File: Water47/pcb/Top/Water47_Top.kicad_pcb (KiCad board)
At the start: 2 copper layers, 260 x 76.5 mm, 53 parts, among them SW1 Esc, SW10 O, SW11 P, SW12 -, SW13 Del, SW14 Cmd, SW15 A, SW16 S, SW17 D, SW18 F, SW19 G, SW2 Q, SW20 H, SW21 J, SW22 K, SW23 L, SW24 ;, SW25 Bs, SW26 Shift(L), SW27 Z, SW28 X, SW29 C, SW3 W, SW30 V, SW31 B, SW32 N, SW33 M, SW34 ,, SW35 ., SW36 Shift(R), SW37 Fn, SW38 Ctrl(L), SW39 Win(L), SW4 E, SW40 Alt(L), SW41 Shift(C), SW42 Fn(C), SW43 Enter, SW44 ←, SW45 ↓, SW46 ↑, SW47 →, SW5 R, SW6 T, SW7 Y, SW8 U, SW9 I

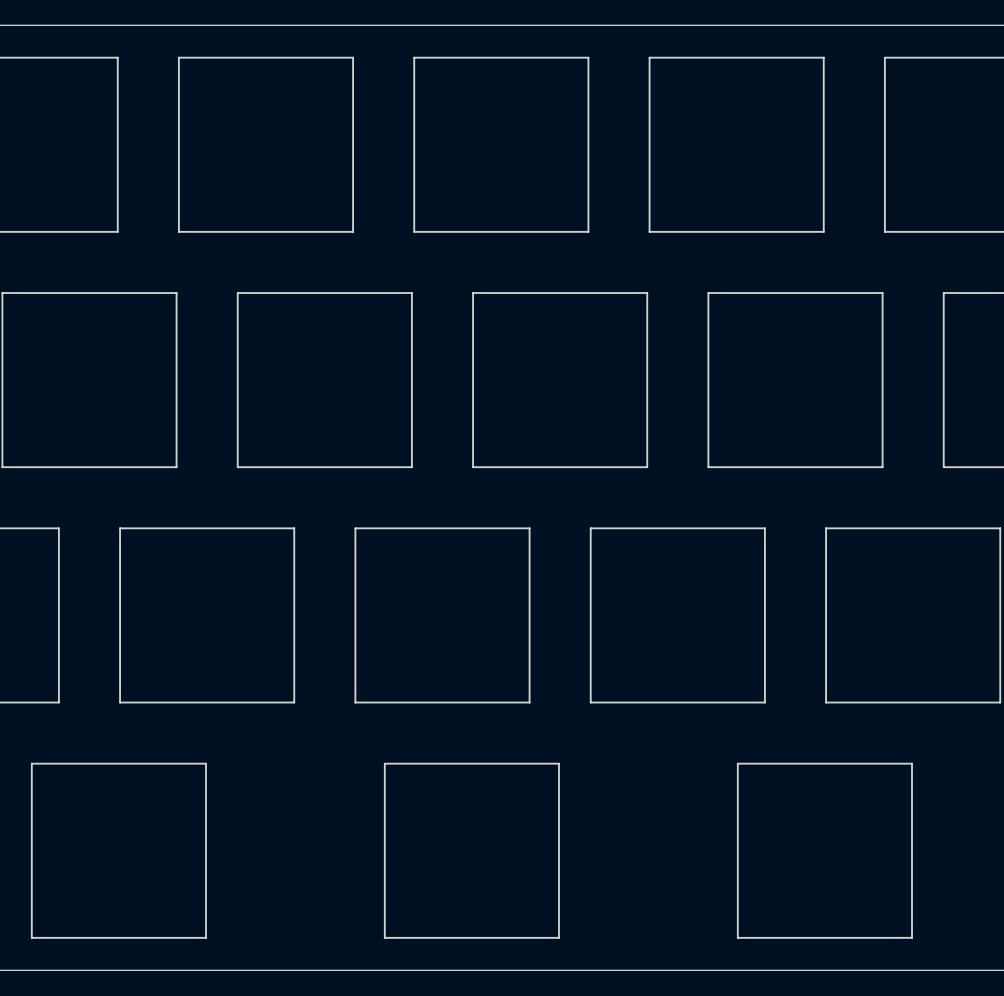
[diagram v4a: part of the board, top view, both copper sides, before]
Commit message: feat: add logo on Top
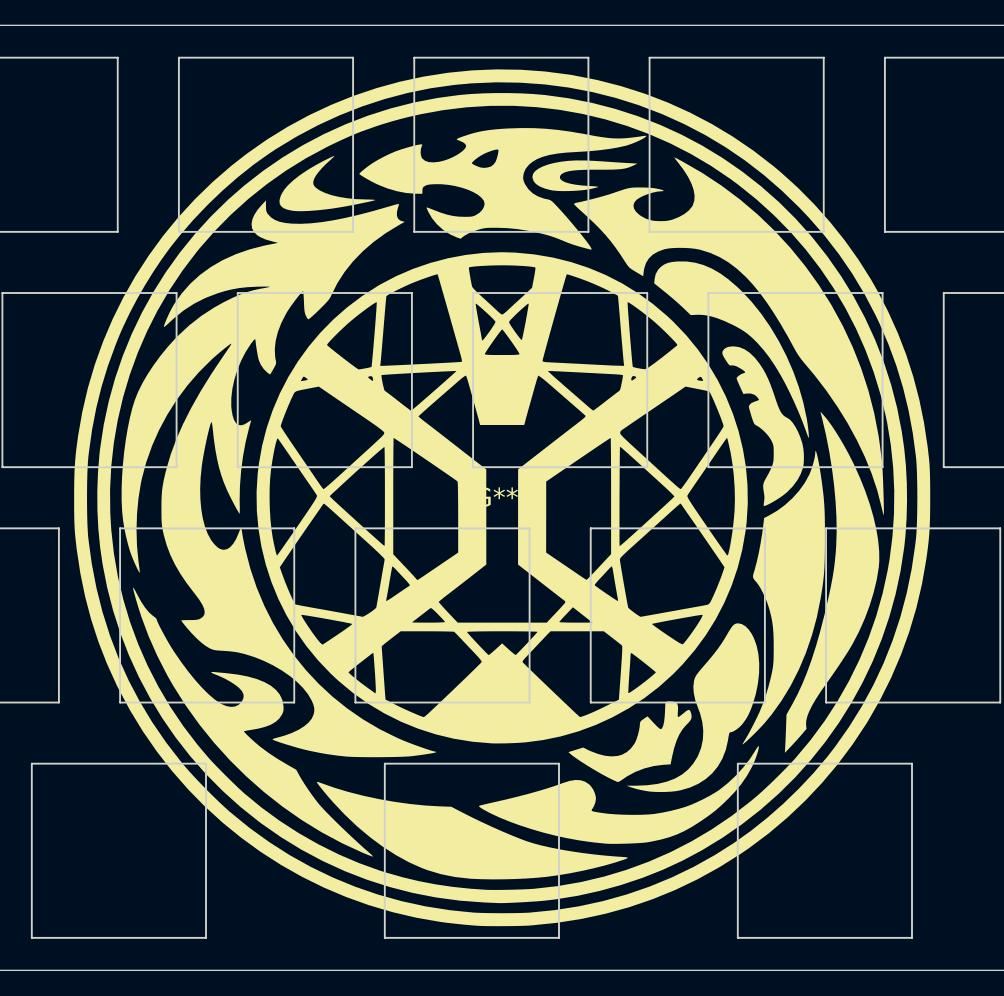
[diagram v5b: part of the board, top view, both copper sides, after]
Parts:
- added G***: LOGO, Silk_Wizard_logos:silk_wizard_logo_70x70, F.Cu at (212.0, 121.5)

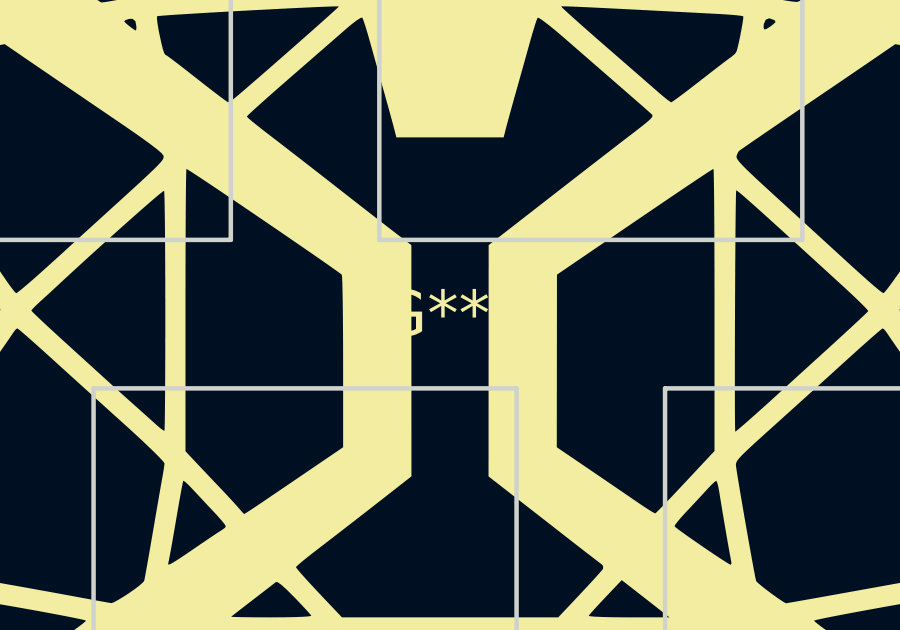
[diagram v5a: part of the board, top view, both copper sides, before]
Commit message: fix: invisible redundant silkscreen
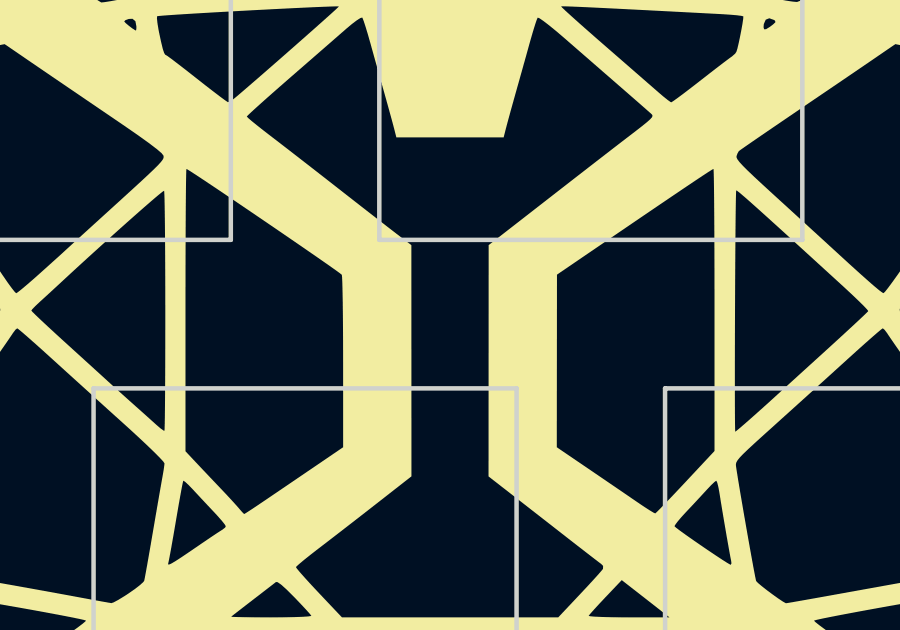
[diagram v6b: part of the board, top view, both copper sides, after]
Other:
- board text added: "Water47 ver1.1 @Top Designed by multifeb13"
- board text removed: "Water47 ver1.0 @Top Designed by multifeb13"
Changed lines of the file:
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@@
     (at 212 121.45)
     (attr board_only exclude_from_pos_files exclude_from_bom)
-    (fp_text reference "G***" (at 0 0) (layer "F.SilkS")
+    (fp_text reference "G***" (at 0 0) (layer "F.SilkS") hide
       (effects (font (size 1.524 1.524) (thickness 0.3)))
     )
@@
   (gr_line (start 340 83.2) (end 84 83.2) (layer "Edge.Cuts") (width 0.1))
   (gr_arc (start 84 159.7) (mid 82.585786 159.114214) (end 82 157.7) (layer "Edge.Cuts") (width 0.1))
-  (gr_text "Water47 ver1.0 @Top Designed by multifeb13" (at 339 153 90) (layer "B.SilkS")
+  (gr_text "Water47 ver1.1 @Top Designed by multifeb13" (at 339 153 90) (layer "B.SilkS")
     (effects (font (size 1 1) (thickness 0.125)) (justify right mirror))
   )
